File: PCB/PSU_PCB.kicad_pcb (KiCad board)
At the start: 2 copper layers, 169.3 x 128 mm, 130 parts, among them CON1 BARREL_JACK, IC1 ATMEGA328-P, P1 USB_OTG, P2 FTDI, P3 V+, P4 V-, P5 ISP, P6 I2C, P7 LCD_Display, Q1 TIP32CG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

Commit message: Small schematic fixes + added backpanel design
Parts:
- removed G***: OSHW-logo_silkscreen-back_12mm, OSHW-logo:OSHW-logo_silkscreen-back_12mm
- removed G*** (x2): LOGO, Lightning:Lightning
- removed R37: 1.8k, Resistors_ThroughHole:Resistor_Horizontal_RM10mm
- added D8: SS34, Diodes_SMD:D_SMB_Handsoldering, F.Cu at (148.1, 133.5)
- D3: footprint Resistors_ThroughHole:Resistor_Horizontal_RM15mm -> Diodes_ThroughHole:D_DO-15_P15.24mm_Horizontal
- R28: value 1.8k -> 2.2k
- R39: value 1k -> 100R
- R48: value 1.8k -> 2.2k; footprint Resistors_ThroughHole:R_Axial_DIN0204_L3.6mm_D1.6mm_P7.62mm_Horizontal -> Resistors_ThroughHole:R_Axial_DIN0207_L6.3mm_D2.5mm_P10.16mm_Horizontal
- R50: value 1k -> 620R
- moved R48 0.93 mm to (167.9, 84.9)
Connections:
- Q1 pad 2: Net-(BT1-Pad1) -> Net-(D8-Pad2)
- Q2 pad 1: VEE -> GND
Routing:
- net VEE: track 108.8 -> 50.2 mm
- net Net-(D8-Pad2): track 0.00 -> 30.7 mm
- net Net-(Q2-Pad2): track 33.7 -> 17.3 mm
- net Net-(BT1-Pad1): track 100.5 -> 92.1 mm
- net Net-(C11-Pad1): track 138.8 -> 137.0 mm
- net Net-(R48-Pad2): track 30.0 -> 28.4 mm

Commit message: Updated BOM
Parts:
- removed 1N4007: D, Diodes_ThroughHole:D_DO-41_SOD81_P10.16mm_Horizontal
- added D9: 1N4007, Diodes_ThroughHole:D_DO-41_SOD81_P10.16mm_Horizontal, F.Cu at (159.3, 69.2)
- C21: footprint Capacitors_ThroughHole:C_Disc_D3.0mm_W1.6mm_P2.50mm -> Capacitors_ThroughHole:C_Rect_L7.0mm_W2.5mm_P5.00mm
- moved C21 4.29 mm to (73.6, 42.3), turned to 180 degrees
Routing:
- net GND: track 102.8 -> 108.3 mm
- net Net-(C21-Pad1): track 139.0 -> 138.5 mm

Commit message: Changed battery monitor resistors
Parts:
- R27: value 6k8 -> 680k
- R28: value 2.2k -> 220k
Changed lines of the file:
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@@
   (general
     (links 296)
-    (no_connects 0)
-    (area 47.694999 26.994999 216.995001 155.005001)
+    (no_connects 69)
+    (area 47.534999 26.994999 216.995001 155.286001)
     (thickness 1.6)
     (drawings 81)
@@
   )
   (setup
-    (last_trace_width 0.381)
+    (last_trace_width 0.25)
     (user_trace_width 0.001)
     (user_trace_width 0.254)
@@
       (effects (font (size 1 1) (thickness 0.15)))
     )
-    (fp_text value 6k8 (at 5.0735 -0.6295 180) (layer F.Fab)
+    (fp_text value 680k (at 5.0735 -0.6295 180) (layer F.Fab)
       (effects (font (size 1 1) (thickness 0.15)))
     )
@@
       (effects (font (size 1 1) (thickness 0.15)))
     )
-    (fp_text value 2.2k (at 5.08 0.635) (layer F.Fab)
+    (fp_text value 220k (at 5.08 0.635) (layer F.Fab)
       (effects (font (size 1 1) (thickness 0.15)))
     )
@@
     )
   )
-  (zone (net 1) (net_name GND) (layer F.Cu) (hatch edge 0.508)
+  (zone (net 1) (net_name GND) (layer B.Cu) (hatch edge 0.508)
     (connect_pads (clearance 0.508))
     (min_thickness 0.254)
-    (fill yes (arc_segments 16) (thermal_gap 0.508) (thermal_bridge_width 0.508))
+    (fill (arc_segments 16) (thermal_gap 0.508) (thermal_bridge_width 0.508))
     (polygon
       (pts
@@
     )
   )
-  (zone (net 1) (net_name GND) (layer B.Cu) (hatch edge 0.508)
+  (zone (net 1) (net_name GND) (layer F.Cu) (hatch edge 0.508)
     (connect_pads (clearance 0.508))
     (min_thickness 0.254)
-    (fill yes (arc_segments 16) (thermal_gap 0.508) (thermal_bridge_width 0.508))
+    (fill (arc_segments 16) (thermal_gap 0.508) (thermal_bridge_width 0.508))
     (polygon
       (pts

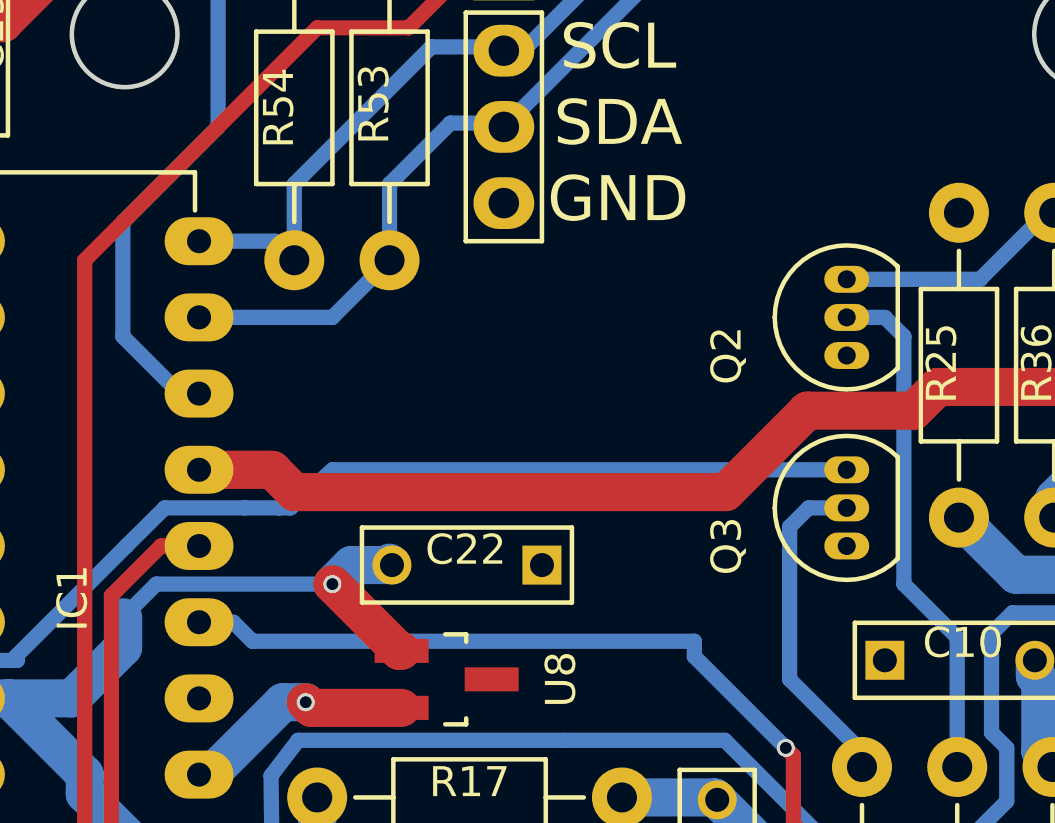
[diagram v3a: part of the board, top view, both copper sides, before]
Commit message: Added autocalibration resistors
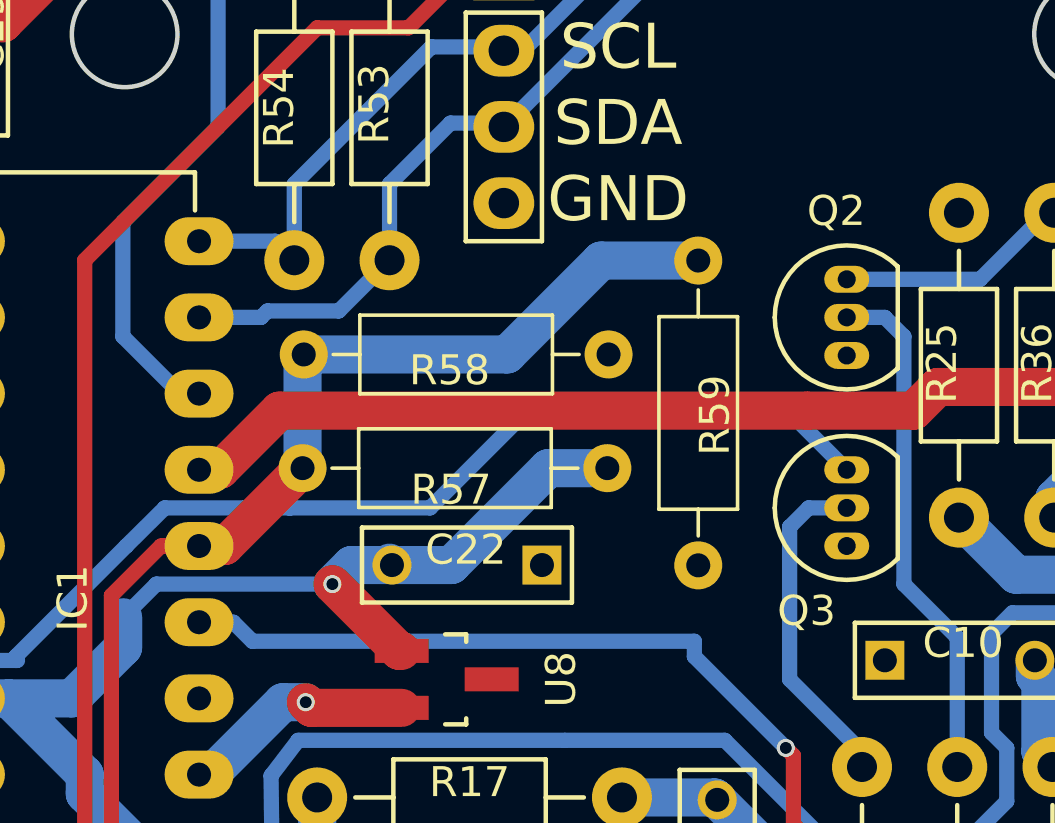
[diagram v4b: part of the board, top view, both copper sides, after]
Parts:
- added R57: 10k 0.1%, Resistors_ThroughHole:R_Axial_DIN0207_L6.3mm_D2.5mm_P10.16mm_Horizontal, F.Cu at (82.6, 70.0)
- added R58: 10k 0.1%, Resistors_ThroughHole:R_Axial_DIN0207_L6.3mm_D2.5mm_P10.16mm_Horizontal, F.Cu at (92.8, 66.2)
- added R59: 10k 0.1%, Resistors_ThroughHole:R_Axial_DIN0207_L6.3mm_D2.5mm_P10.16mm_Horizontal, F.Cu at (95.8, 73.2)
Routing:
- net Pot: track 130.1 -> 152.8 mm
- net +5V: track 457.9 -> 466.4 mm
- net Net-(D2-Pad1): track 57.9 -> 59.7 mm
- net ADC_Iout: track 82.5 -> 81.9 mm
